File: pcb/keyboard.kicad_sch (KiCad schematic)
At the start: 60 parts, among them J1 Tag-Connect TC2030, J1 USB4510-03-1-A, J4 Battery, Q2 2N7002, SW1 PWR, U1 SRV05-4, U3 BQ24075, U3 BT840, Y1 ECS-.327-9-34B-TR

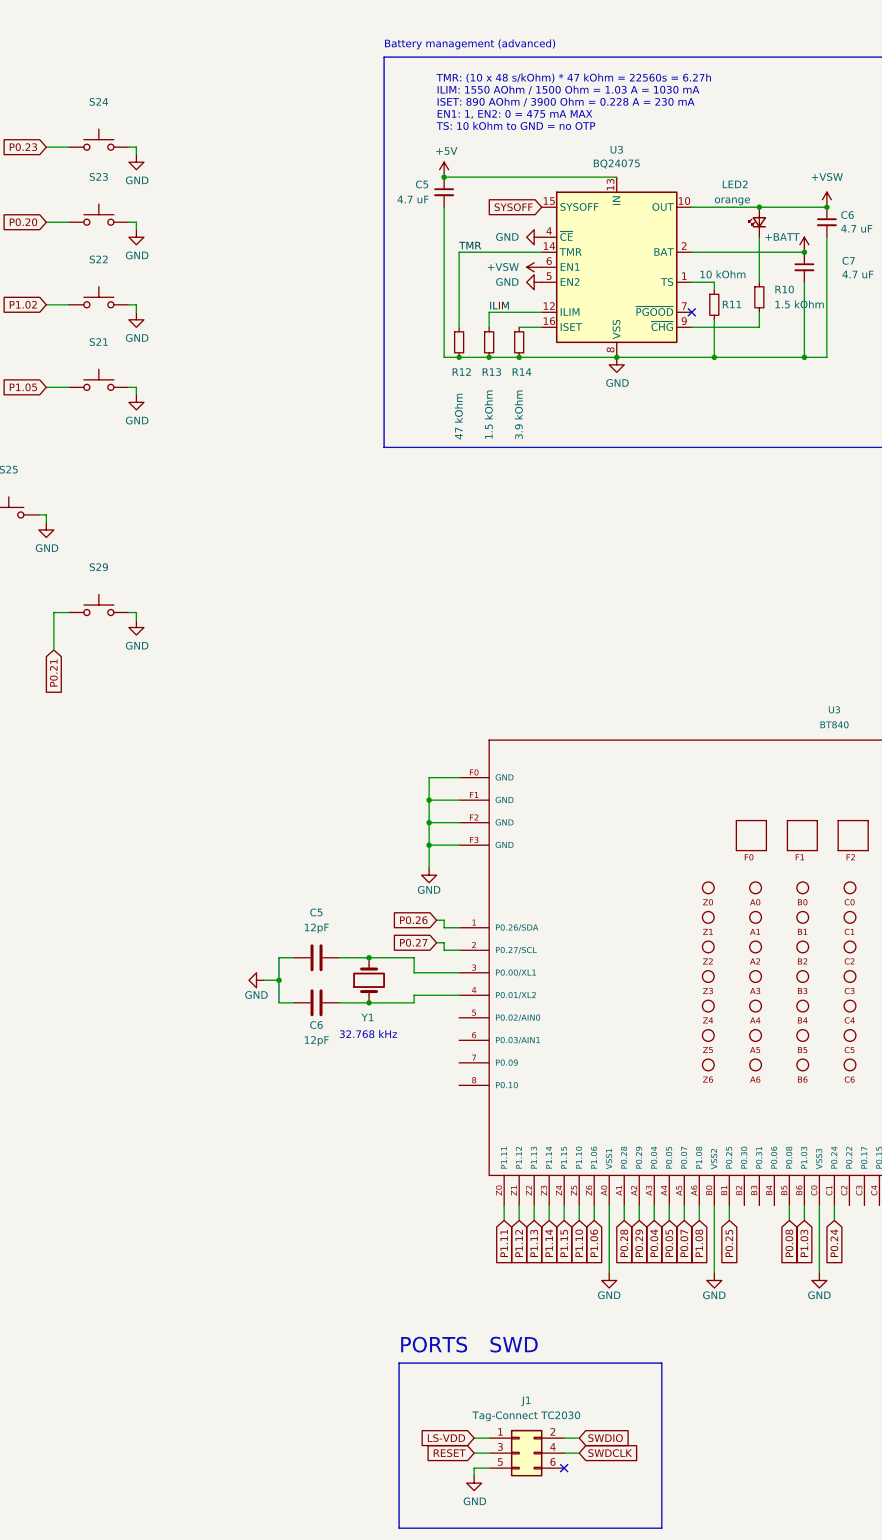
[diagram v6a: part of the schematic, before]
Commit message: #1 Select Battery and Battery Connector
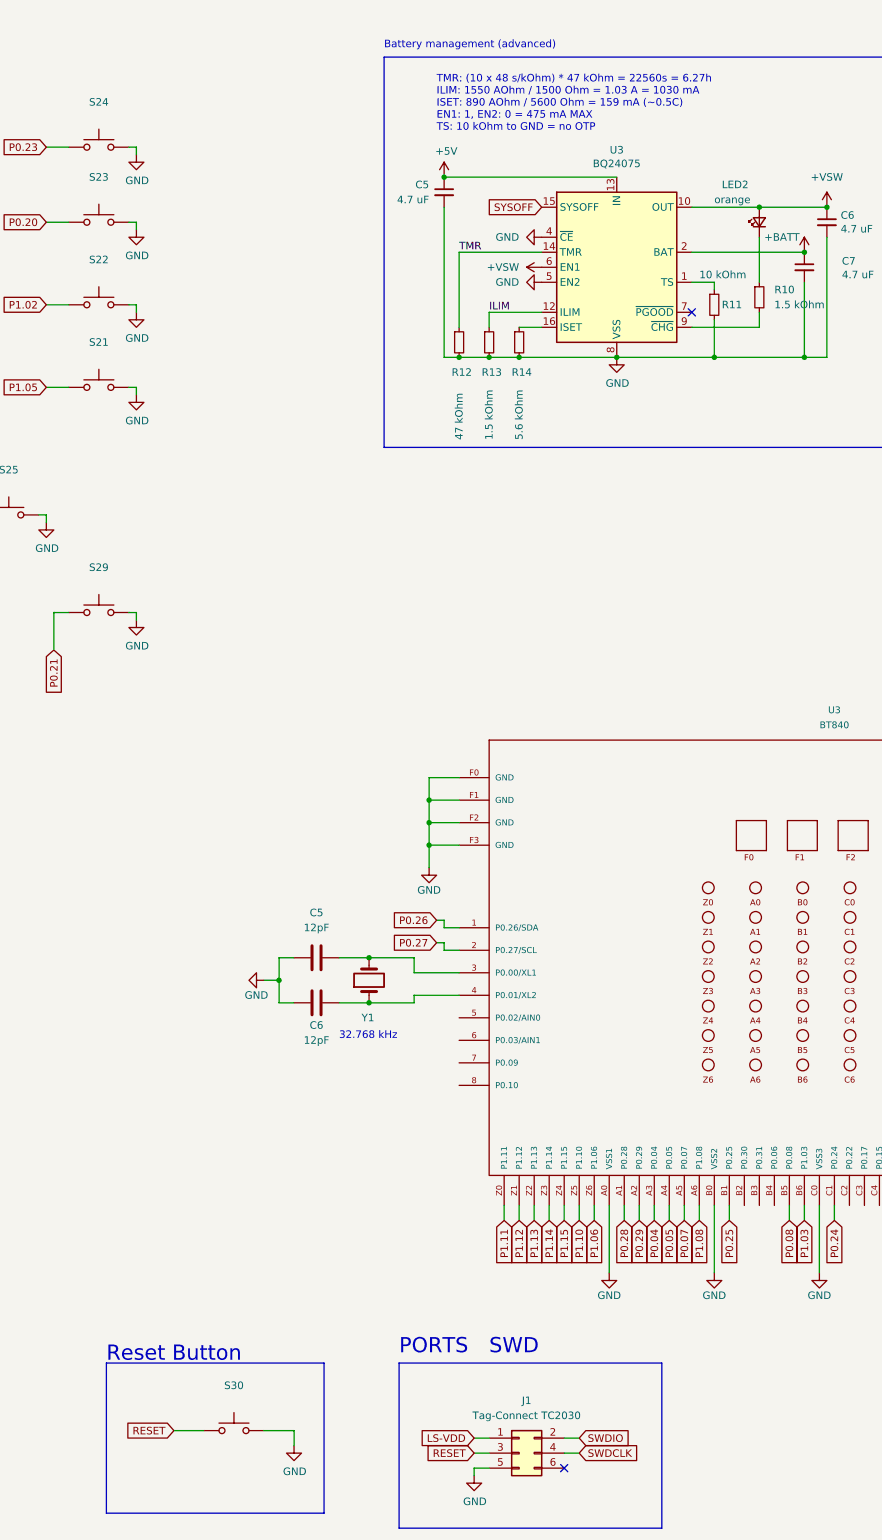
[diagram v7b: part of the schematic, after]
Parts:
- added S30: ~, symbol Switch:SW_Push
- R14: value 3.9 kOhm -> 5.6 kOhm
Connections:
- net GND: now also S30.2
- net RESET: now also S30.1
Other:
- note added: "Reset Button"
- note added: "TMR: (10 x 48 s/kOhm) * 47 kOhm = 22560s = 6.27h ILIM: 1550 AOhm / 1500 Ohm = 1.03 A = 1030 mA ISET: 890 AOhm / 5600 Ohm = 159 mA (~0.5C) EN1: 1, EN2: 0 = 475 mA MAX TS: 10 kOhm to GND = no OTP"
- note removed: "TMR: (10 x 48 s/kOhm) * 47 kOhm = 22560s = 6.27h ILIM: 1550 AOhm / 1500 Ohm = 1.03 A = 1030 mA ISET: 890 AOhm / 3900 Ohm = 0.228 A = 230 mA EN1: 1, EN2: 0 = 475 mA MAX TS: 10 kOhm to GND = no OTP"
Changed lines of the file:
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@@
     (stroke (width 0) (type default))
   )
+  (wire (pts (xy 227.33 260.35) (xy 227.33 262.89))
+    (stroke (width 0) (type default))
+  )
   (wire (pts (xy 351.79 222.25) (xy 351.79 224.79))
     (stroke (width 0) (type default))
@@
     (stroke (width 0) (type default))
   )
+  (wire (pts (xy 207.01 260.35) (xy 212.09 260.35))
+    (stroke (width 0) (type default))
+  )
   (wire (pts (xy 278.13 222.25) (xy 278.13 224.79))
     (stroke (width 0) (type default))
@@
     (stroke (width 0) (type default))
   )
+  (wire (pts (xy 222.25 260.35) (xy 227.33 260.35))
+    (stroke (width 0) (type default))
+  )
   (wire (pts (xy 166.37 36.83) (xy 166.37 38.1))
     (stroke (width 0) (type default))
@@
     (stroke (width 0) (type default))
   )
+  (rectangle (start 195.58 248.92) (end 232.41 274.32)
+    (stroke (width 0) (type default))
+    (fill (type none))
+  )
   (text "USB connectors and protections" (at 21.59 208.28 0)
     (effects (font (size 1.27 1.27)) (justify left bottom))
   )
-  (text "TMR: (10 x 48 s/kOhm) * 47 kOhm = 22560s = 6.27h\nILIM: 1550 AOhm / 1500 Ohm = 1.03 A = 1030 mA\nISET: 890 AOhm / 3900 Ohm = 0.228 A = 230 mA\nEN1: 1, EN2: 0 = 475 mA MAX\nTS: 10 kOhm to GND = no OTP"
+  (text "Reset Button" (at 195.58 248.92 0)
+    (effects (font (size 2.5654 2.5654)) (justify left bottom))
+  )
+  (text "TMR: (10 x 48 s/kOhm) * 47 kOhm = 22560s = 6.27h\nILIM: 1550 AOhm / 1500 Ohm = 1.03 A = 1030 mA\nISET: 890 AOhm / 5600 Ohm = 159 mA (~0.5C)\nEN1: 1, EN2: 0 = 475 mA MAX\nTS: 10 kOhm to GND = no OTP"
     (at 251.46 40.64 0)
     (effects (font (size 1.27 1.27)) (justify left bottom))
@@
     )
   )
+  (global_label "RESET" (shape input) (at 207.01 260.35 180) (fields_autoplaced)
+    (effects (font (size 1.27 1.27)) (justify right))
+    (property "Intersheetrefs" "${INTERSHEET_REFS}" (at 264.16 434.34 0)
+      (effects (font (size 1.27 1.27)) hide)
+    )
+  )
   (global_label "P1.01" (shape input) (at 346.71 224.79 270) (fields_autoplaced)
     (effects (font (size 1.27 1.27)) (justify right))
@@
       (effects (font (size 1.27 1.27)) (justify left))
     )
-    (property "Value" "3.9 kOhm" (at 265.43 92.71 90)
+    (property "Value" "5.6 kOhm" (at 265.43 92.71 90)
       (effects (font (size 1.27 1.27)) (justify left))
     )
@@
     )
   )
+  (symbol (lib_id "power:GND") (at 227.33 262.89 0) (unit 1)
+    (in_bom yes) (on_board yes) (dnp no)
+    (property "Reference" "#PWR04" (at 227.33 269.24 0)
+      (effects (font (size 1.27 1.27)) hide)
+    )
+    (property "Value" "GND" (at 227.457 267.2842 0)
+      (effects (font (size 1.27 1.27)))
+    )
+    (property "Footprint" "" (at 227.33 262.89 0)
+      (effects (font (size 1.27 1.27)) hide)
+    )
+    (property "Datasheet" "" (at 227.33 262.89 0)
+      (effects (font (size 1.27 1.27)) hide)
+    )
+    (pin "1")
+    (instances
+      (project "LH2-mini-mote"
+        (path "/6fd53a87-94b7-4171-b15d-b0155e39189b"
+          (reference "#PWR04") (unit 1)
+        )
+      )
+      (project "keyboard"
+        (path "/cf0c78e1-ddbc-47c3-b3dc-2a4f1ccfd0ad"
+          (reference "#PWR059") (unit 1)
+        )
+      )
+    )
+  )
   (symbol (lib_id "Device:R_Small") (at 341.63 49.53 0) (unit 1)
     (in_bom yes) (on_board yes) (dnp no) (fields_autoplaced)
@@
         )
       )
+    )
+  )
+  (symbol (lib_id "Switch:SW_Push") (at 217.17 260.35 0) (unit 1)
+    (in_bom yes) (on_board yes) (dnp no) (fields_autoplaced)
+    (property "Reference" "S30" (at 217.17 252.73 0)
+      (effects (font (size 1.27 1.27)))
+    )
+    (property "Value" "~" (at 217.17 255.27 0)
+      (effects (font (size 1.27 1.27)))
+    )
+    (property "Footprint" "" (at 217.17 255.27 0)
+      (effects (font (size 1.27 1.27)) hide)
+    )
+    (property "Datasheet" "~" (at 217.17 255.27 0)
+      (effects (font (size 1.27 1.27)) hide)
+    )
+    (property "Digikey" "" (at 217.17 260.35 0)
+      (effects (font (size 1.27 1.27)) hide)
+    )
+    (pin "2")
+    (pin "1")
+    (instances
+      (project "keyboard"
+        (path "/cf0c78e1-ddbc-47c3-b3dc-2a4f1ccfd0ad"
+          (reference "S30") (unit 1)
+        )
+      )

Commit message: #1 Select power switch
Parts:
- J4: value Battery -> Battery (JST_S2B-PH-K-S); Digikey (none) -> https://www.digikey.fr/short/4nfzf328
- SW1: footprint PCM_marbastlib-various:SW_MSK12C02-HB -> keyboard:SW_SPDT_PCM12; Digikey (none) -> https://www.digikey.fr/short/pnt4qtt1; Mfr Part Number (none) -> PCM12SMTR
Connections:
- net ILIM: no longer names the net of R13.1, U3.12 (ILIM)
- net TMR: no longer names the net of R12.1, U3.14 (TMR)
